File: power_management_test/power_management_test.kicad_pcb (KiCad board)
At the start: 2 copper layers, 65 x 67.4 mm, 52 parts, among them J1 Conn_01x02_Socket, J2 Conn_01x02_Socket, J3 Conn_01x02_Socket, J4 Conn_01x02_Socket, J5 Conn_01x06_Pin, J505 Conn_01x01_Socket, J6 Conn_01x02_Socket, J7 Conn_01x02_Socket, U503 INA169, U504 MCP6002T-E/OT

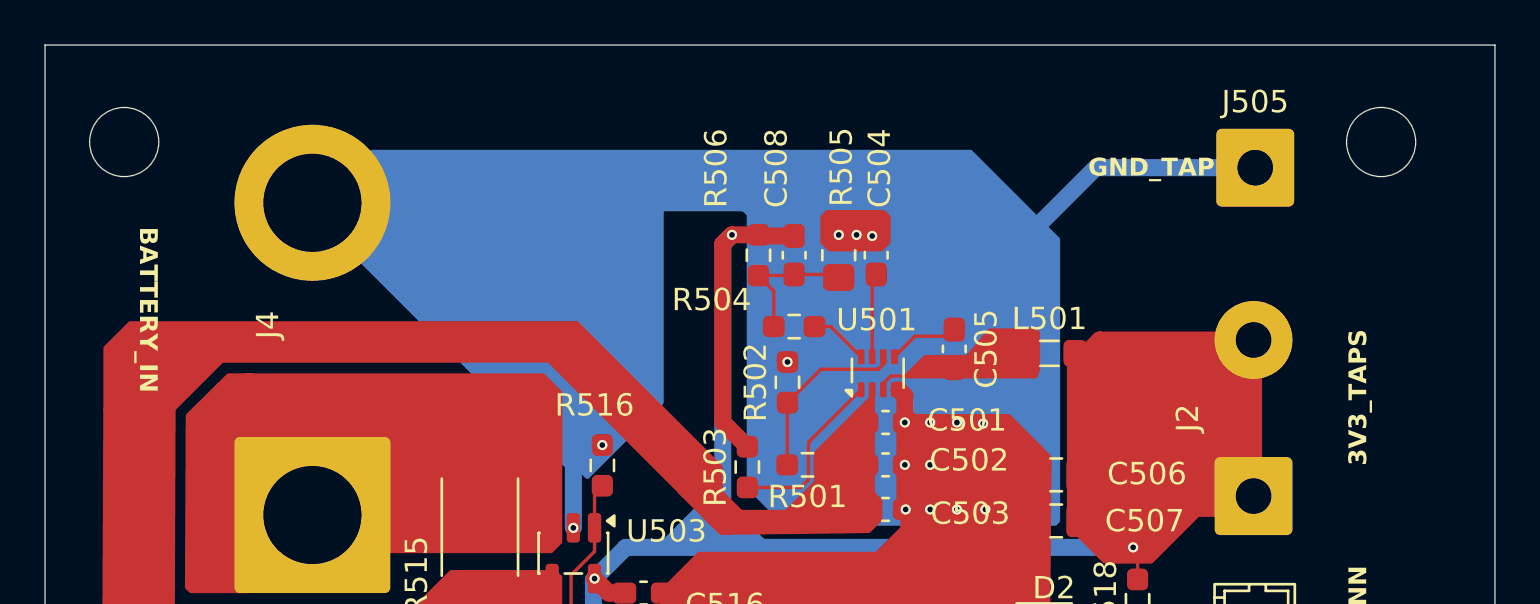
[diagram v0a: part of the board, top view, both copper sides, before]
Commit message: Updated BOM and fixed minor mismatches
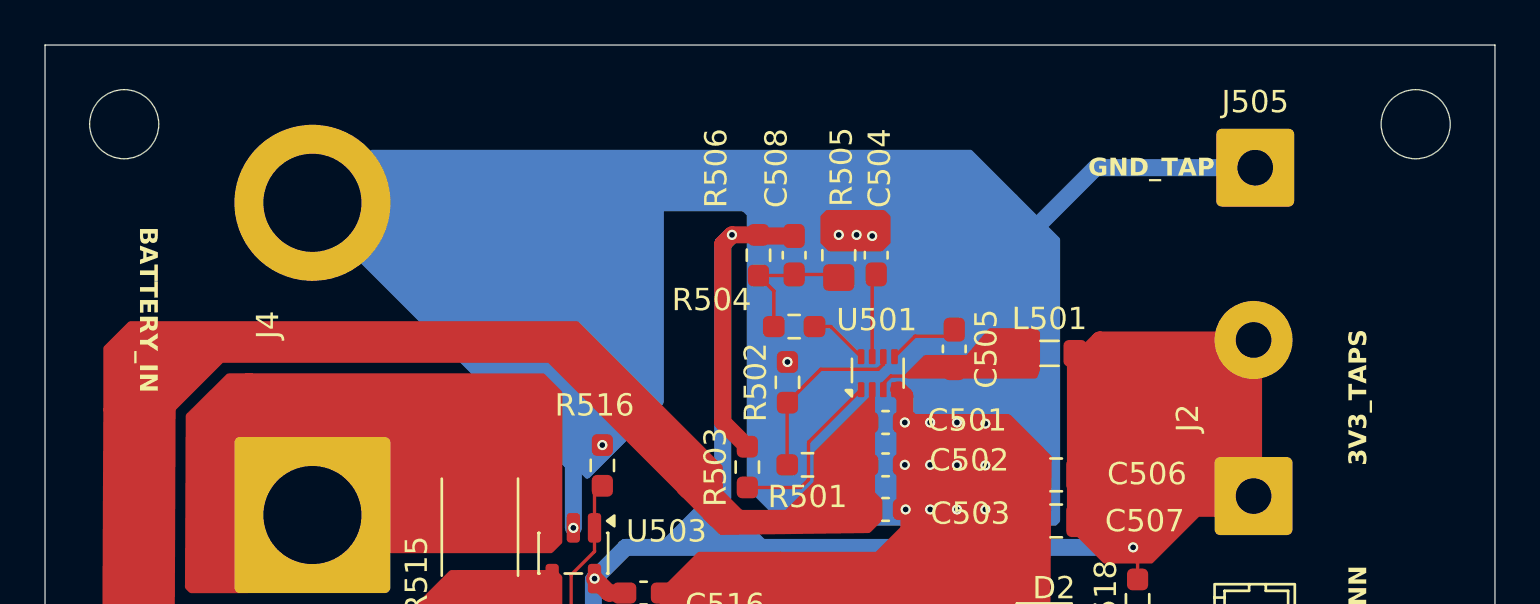
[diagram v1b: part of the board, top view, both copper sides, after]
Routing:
- net GND: vias 54 -> 56
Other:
- outline, holes or cut-outs redrawn
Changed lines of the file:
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@@
 		)
 		(property "Value" "1K ±1%"
-			(at 0 1.43 90)
+			(at 0 1.75 90)
 			(layer "F.Fab")
 			(effects
@@
 	)
 	(gr_circle
-		(center 116.36 42.55)
-		(end 117.91 42.55)
+		(center 116.36 41.75)
+		(end 117.91 41.75)
 		(stroke
 			(width 0.0381)
@@
 	)
 	(gr_circle
-		(center 172.72 42.55)
-		(end 174.27 42.55)
+		(center 174.27 41.75)
+		(end 175.82 41.75)
 		(stroke
 			(width 0.0381)
@@
 	)
 	(via
-		(at 154.875 55.175)
+		(at 154.975 55.175)
 		(size 0.4572)
 		(drill 0.254)
@@
 	)
 	(via
+		(at 153.7 57.04)
+		(size 0.4572)
+		(drill 0.254)
+		(layers "F.Cu" "B.Cu")
+		(net 2)
+	)
+	(via
 		(at 156.35 70.425)
 		(size 0.4572)
@@
 	)
 	(via
+		(at 154.975 57.05)
+		(size 0.4572)
+		(drill 0.254)
+		(layers "F.Cu" "B.Cu")
+		(net 2)
+	)
+	(via
 		(at 152.605 69.67)
 		(size 0.4572)
@@
 			"679284fa-f116-4037-9033-936ca5f49932" "68314656-bb3b-4fb5-81dc-23c74f575226"
 			"698a6930-56ab-4c7f-bbcf-b6e783ebc6c7" "6cacf41c-fdf1-4c91-808a-ab35c01efb00"
-			"6d03517e-98f5-4965-a1ff-4bb561df1ccf" "75bce750-dc16-4c29-96a1-e55c99cd753f"
-			"76ff59b6-bdb9-4ee5-bd88-98614829ab55" "7c2aad7e-4f61-4fee-8d22-193b2fda1413"
-			"7d94a0c6-e700-4f01-b273-26b251cfd69c" "7f6bbad4-21d3-4b2c-9840-d1d71c267418"
-			"805bae53-9bb4-40e0-b01f-ea7e2b2b2be4" "83a35f73-584a-4fe8-b6cc-5fd4995108a6"
-			"85853fd9-e3e6-4343-b8e7-f3e5fa30194d" "8593d987-0a89-4e69-a862-49239f76fa10"
-			"88aecfcb-98b6-4834-853c-bda51cd0de7b" "8acbbf5b-ab8e-44c1-aad5-5d53b1eccedc"
-			"8d608e4b-4501-4514-b2fe-f0d025f3d54e" "8fab6524-5f5f-47f3-9e66-a8ca4bad1fbd"
-			"8fee475b-c6a7-4e49-84d6-82f4c07876a4" "90a4a13b-63bf-44fe-a234-9bee60a90865"
-			"98ca69bb-6327-42cc-95b2-dd71ab7fcf6a" "98e86bba-b816-471a-8155-a6f8ac221e02"
-			"a02ad088-c190-46c6-9054-a5127999e304" "a4468a34-2b1b-4466-a483-4c178fc54412"
-			"a4a0d5c5-15dc-43de-9b64-6aba33e9cce0" "a5fb4d26-38ac-4b3e-bc56-230ab191903f"
+			"6d03517e-98f5-4965-a1ff-4bb561df1ccf" "6ff23fcc-37d8-4d8e-a250-ef205f97c026"
+			"75bce750-dc16-4c29-96a1-e55c99cd753f" "76ff59b6-bdb9-4ee5-bd88-98614829ab55"
+			"7c2aad7e-4f61-4fee-8d22-193b2fda1413" "7d94a0c6-e700-4f01-b273-26b251cfd69c"
+			"7f6bbad4-21d3-4b2c-9840-d1d71c267418" "805bae53-9bb4-40e0-b01f-ea7e2b2b2be4"
+			"83a35f73-584a-4fe8-b6cc-5fd4995108a6" "85853fd9-e3e6-4343-b8e7-f3e5fa30194d"
+			"8593d987-0a89-4e69-a862-49239f76fa10" "88aecfcb-98b6-4834-853c-bda51cd0de7b"
+			"8acbbf5b-ab8e-44c1-aad5-5d53b1eccedc" "8d608e4b-4501-4514-b2fe-f0d025f3d54e"
+			"8fab6524-5f5f-47f3-9e66-a8ca4bad1fbd" "8fee475b-c6a7-4e49-84d6-82f4c07876a4"
+			"90a4a13b-63bf-44fe-a234-9bee60a90865" "98ca69bb-6327-42cc-95b2-dd71ab7fcf6a"
+			"98e86bba-b816-471a-8155-a6f8ac221e02" "a02ad088-c190-46c6-9054-a5127999e304"
+			"a4468a34-2b1b-4466-a483-4c178fc54412" "a4a0d5c5-15dc-43de-9b64-6aba33e9cce0"
+			"a5fb4d26-38ac-4b3e-bc56-230ab191903f" "a91910eb-511e-49c2-b7c4-7f52f526714e"
 			"aaed1b2b-a6b0-4b21-96c3-5ffc994fa78b" "ac5a40e7-2e43-439a-b7c7-b5cb99fb4354"
 			"b233dc88-5016-45ac-a83a-467caf2b49c6" "b4d442ac-2e01-413e-8ccc-066d89dcbc97"

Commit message: Final Check
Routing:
- net Net-(U504B-+): track 19.8 -> 18.3 mm
- net /V_bat: track 111.6 -> 112.6 mm
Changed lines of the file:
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@@
 		(tenting front back)
 		(pcbplotparams
-			(layerselection 0x00000000_00000000_55555555_5755f5ff)
-			(plot_on_all_layers_selection 0x00000000_00000000_00000000_00000000)
+			(layerselection 0x00000000_00000000_5555555f_5755ffff)
+			(plot_on_all_layers_selection 0x00000000_00000000_00000000_02000000)
 			(disableapertmacros no)
 			(usegerberextensions no)
 			(usegerberattributes yes)
 			(usegerberadvancedattributes yes)
-			(creategerberjobfile yes)
+			(creategerberjobfile no)
 			(dashed_line_dash_ratio 12.000000)
 			(dashed_line_gap_ratio 3.000000)
@@
 			(plotframeref no)
 			(mode 1)
-			(useauxorigin no)
+			(useauxorigin yes)
 			(hpglpennumber 1)
 			(hpglpenspeed 20)
@@
 			(psa4output no)
 			(plot_black_and_white yes)
-			(sketchpadsonfab no)
-			(plotpadnumbers no)
+			(sketchpadsonfab yes)
+			(plotpadnumbers yes)
 			(hidednponfab no)
 			(sketchdnponfab yes)
@@
 			(outputformat 1)
 			(mirror no)
-			(drillshape 1)
+			(drillshape 0)
 			(scaleselection 1)
-			(outputdirectory "")
+			(outputdirectory "/Users/ericoliviera/Desktop/VAK/Loam/power_management_test/Gerbers_And_Drills/")
 		)
 	)
@@
 		(tags "resistor handsolder")
 		(property "Reference" "R515"
-			(at 2.177064 2.84 270)
+			(at -4.73 0 0)
 			(layer "F.SilkS")
 			(effects
@@
 		(tags "SOT TO_SOT_SMD")
 		(property "Reference" "U503"
-			(at -0.9875 -4.175 180)
+			(at -0.9875 -4.175 0)
 			(layer "F.SilkS")
 			(effects
@@
 		)
 		(property "Value" "INA169"
-			(at 0.3225 -4.45 180)
+			(at 0.3225 -4.45 0)
 			(layer "F.Fab")
 			(effects
@@
 	(gr_poly
 		(pts
-			(xy 135.13 53.05) (xy 135.88 53.8) (xy 135.88 60.47) (xy 135.49 60.86) (xy 128.35 60.86) (xy 127.48 59.99)
-			(xy 127.48 58.25) (xy 125.25 56.02) (xy 122.12 56.02) (xy 122.07 55.97) (xy 122.07 53.05) (xy 122.13 53.05)
+			(xy 134.95 53.05) (xy 135.88 53.98) (xy 135.88 60.47) (xy 135.4 60.95) (xy 128.44 60.95) (xy 127.48 59.99)
+			(xy 127.48 58.25) (xy 125.25 56.02) (xy 122.12 56.02) (xy 122.07 55.97) (xy 122.07 53.05) (xy 122.17 53.05)
 		)
 		(stroke
@@
 	(gr_poly
 		(pts
-			(xy 123.64 67.448665) (xy 126.79 64.298665) (xy 126.621335 64.13) (xy 119.55 64.13) (xy 118.630319 65.049681)
+			(xy 123.64 67.448665) (xy 126.79 64.298665) (xy 126.198606 63.707271) (xy 118.648908 63.737581) (xy 118.630319 65.049681)
 			(xy 118.630319 67.473669) (xy 123.73 67.473669) (xy 123.65 67.473669) (xy 123.64 67.463669)
 		)
@@
 	(gr_poly
 		(pts
+			(xy 121.139454 53.148868) (xy 122.015789 52.25) (xy 134.15 52.25) (xy 134.951261 53.051261)
+		)
+		(stroke
+			(width 0.254)
+			(type solid)
+		)
+		(fill yes)
+		(layer "F.Cu")
+		(net 13)
+	)
+	(gr_poly
+		(pts
 			(xy 151.375 80.075) (xy 151.5 89.325) (xy 157.85 89.325) (xy 157.875 83.35) (xy 157.9 81.65) (xy 156.2 79.975)
 		)
@@
 	(gr_poly
 		(pts
-			(xy 115.55 54.55) (xy 115.55 51.8) (xy 116.64 50.71) (xy 136.655 50.71) (xy 143.07 57.125) (xy 143.07 57.95)
-			(xy 142.64 58.38) (xy 141.48 58.38) (xy 135.42 52.32) (xy 120.73 52.32) (xy 118.5 54.55)
+			(xy 115.55 54.55) (xy 115.55 51.8) (xy 117.61 49.74) (xy 135.685 49.74) (xy 143.07 57.125) (xy 143.07 57.95)
+			(xy 142.64 58.38) (xy 141.48 58.38) (xy 134.51 51.41) (xy 121.64 51.41) (xy 118.5 54.55)
 		)
 		(stroke
@@
 	(gr_poly
 		(pts
-			(xy 135.88 62.08) (xy 135.88 64.11) (xy 134.8 65.19) (xy 126.27 65.19) (xy 126.201335 65.121335)
-			(xy 126.201335 64.13) (xy 128.77 64.13) (xy 131.03 61.87) (xy 135.67 61.87)
+			(xy 135.88 62.08) (xy 135.88 64.11) (xy 134.5 65.49) (xy 126.32 65.49) (xy 125.691335 64.861335)
+			(xy 125.691335 63.71) (xy 128.89 63.71) (xy 130.73 61.87) (xy 135.67 61.87)
 		)
 		(stroke
@@
 	(gr_poly
 		(pts
-			(xy 122.07 53.05) (xy 121.043285 53.05) (xy 119.243964 54.8321) (xy 119.210884 62.505431) (xy 119.364053 62.65)
-			(xy 121.88 62.65) (xy 121.886562 62.65) (xy 121.836562 53.05)
+			(xy 122.156169 53.05) (xy 121.238196 53.05) (xy 119.329663 54.940266) (xy 119.297053 62.505431) (xy 119.450221 62.65)
+			(xy 121.92 62.65) (xy 121.972731 62.65) (xy 121.922731 53.05)
 		)
 		(stroke
@@
 	(gr_poly
 		(pts
+			(xy 128.054934 60.724344) (xy 128.054934 62.65) (xy 128.52301 62.65) (xy 130.327124 60.684344) (xy 128.094934 60.684344)
+		)
+		(stroke
+			(width 0.254)
+			(type solid)
+		)
+		(fill yes)
+		(layer "F.Cu")
+		(net 13)
+	)
+	(gr_poly
+		(pts
 			(xy 159.275 77.675) (xy 159.275 85.155) (xy 160.22 86.1) (xy 162.65 86.1) (xy 166.775 81.975) (xy 166.775 77.775)
 			(xy 165.475 76.475) (xy 160.475 76.475)
@@
 	)
 	(segment
-		(start 116.991748 53.618252)
-		(end 116.991748 65.691748)
+		(start 133.2 64.475)
+		(end 135.55 62.125)
 		(width 0.762)
 		(layer "F.Cu")
@@
 	)
 	(segment
-		(start 133.2 64.475)
-		(end 135.55 62.125)
+		(start 146.173683 59.425)
+		(end 143.9 59.425)
 		(width 0.762)
 		(layer "F.Cu")
@@
 	)
 	(segment
-		(start 125.375 66.0125)
-		(end 121.34375 70.04375)
+		(start 143.9 59.425)
+		(end 134.485 50.01)
 		(width 0.762)
 		(layer "F.Cu")
@@
 	)
 	(segment
-		(start 135.655 51.18)
-		(end 119.43 51.18)
+		(start 125.375 66.0125)
+		(end 121.34375 70.04375)
 		(width 0.762)
 		(layer "F.Cu")
@@
 	)
 	(segment
-		(start 148.65 56.948683)
-		(end 146.173683 59.425)
+		(start 146.063683 84.56)
+		(end 148.725 81.898683)
 		(width 0.762)
 		(layer "F.Cu")
@@
 	)
 	(segment
-		(start 146.063683 84.56)
-		(end 148.725 81.898683)
+		(start 134.485 50.01)
+		(end 120.6 50.01)
 		(width 0.762)
 		(layer "F.Cu")
@@
 	)
 	(segment
-		(start 143.9 59.425)
-		(end 135.655 51.18)
+		(start 148.65 56.948683)
+		(end 146.173683 59.425)
 		(width 0.762)
 		(layer "F.Cu")
@@
 	)
 	(segment
-		(start 146.173683 59.425)
-		(end 143.9 59.425)
+		(start 135.55 62.125)
+		(end 131.38 62.125)
 		(width 0.762)
 		(layer "F.Cu")
@@
 	)
 	(segment
-		(start 135.55 62.125)
-		(end 131.38 62.125)
+		(start 131.38 62.125)
+		(end 131.225 62.28)
 		(width 0.762)
 		(layer "F.Cu")
@@
 	)
 	(segment
-		(start 148.65 56.525)
-		(end 148.65 56.948683)
+		(start 124.275 82.35)
+		(end 126.485 84.56)
 		(width 0.762)
 		(layer "F.Cu")
@@
 	)
 	(segment
-		(start 131.38 62.125)
-		(end 131.225 62.28)
+		(start 149.6375 57.025)
+		(end 149.6375 55.125)
 		(width 0.762)
 		(layer "F.Cu")
@@
 	)
 	(segment
-		(start 119.43 51.18)
-		(end 116.991748 53.618252)
-		(width 0.762)
+		(start 149.975 80.2875)
+		(end 149.6725 80.59)
+		(width 0.254)
 		(layer "F.Cu")
 		(net 1)
 	)
 	(segment
-		(start 124.275 82.35)
-		(end 126.485 84.56)
+		(start 116.991748 53.618252)
+		(end 116.991748 65.691748)
 		(width 0.762)
 		(layer "F.Cu")
@@
 	)
 	(segment
-		(start 149.6375 57.025)
-		(end 149.6375 55.125)
+		(start 120.6 50.01)
+		(end 116.991748 53.618252)
 		(width 0.762)
 		(layer "F.Cu")
@@
 	)
 	(segment
-		(start 149.975 80.2875)
-		(end 149.6725 80.59)
-		(width 0.254)
+		(start 148.65 56.525)
+		(end 148.65 56.948683)
+		(width 0.762)
 		(layer "F.Cu")
 		(net 1)
@@
 	)
 	(segment
-		(start 136.4 64.75)
-		(end 134.075 67.075)
+		(start 137.45 58.3125)
+		(end 137.8 57.9625)
 		(width 0.1524)
 		(layer "F.Cu")
@@
 	)
 	(segment
-		(start 137.45 58.3125)
-		(end 137.8 57.9625)
+		(start 135.8 66.8)
+		(end 135.8 73.22)
 		(width 0.1524)
 		(layer "F.Cu")
@@
 	)
 	(segment
-		(start 134.075 71.495)
-		(end 137.4 74.82)
+		(start 137.45 60.921508)
+		(end 136.35 62.021508)
 		(width 0.1524)
 		(layer "F.Cu")
@@
 	(segment
 		(start 137.45 59.85)
-		(end 137.45 60.9092)
+		(end 137.45 58.3125)
 		(width 0.1524)
 		(layer "F.Cu")
@@
 	)
 	(segment
-		(start 137.45 60.9092)
-		(end 136.4 61.9592)
+		(start 136.35 62.021508)
+		(end 136.35 66.25)
 		(width 0.1524)
 		(layer "F.Cu")
@@
 	)
 	(segment
-		(start 137.45 59.85)
-		(end 137.45 58.3125)
+		(start 136.35 66.25)
+		(end 135.8 66.8)
 		(width 0.1524)
 		(layer "F.Cu")
@@
 	)
 	(segment
-		(start 134.075 67.075)
-		(end 134.075 71.495)
+		(start 137.45 59.85)
+		(end 137.45 60.921508)
 		(width 0.1524)
 		(layer "F.Cu")
@@
 	)
 	(segment
-		(start 136.4 61.9592)
-		(end 136.4 64.75)
+		(start 135.8 73.22)
+		(end 137.4 74.82)
 		(width 0.1524)
 		(layer "F.Cu")
